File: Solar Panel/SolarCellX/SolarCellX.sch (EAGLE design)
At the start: 55 parts

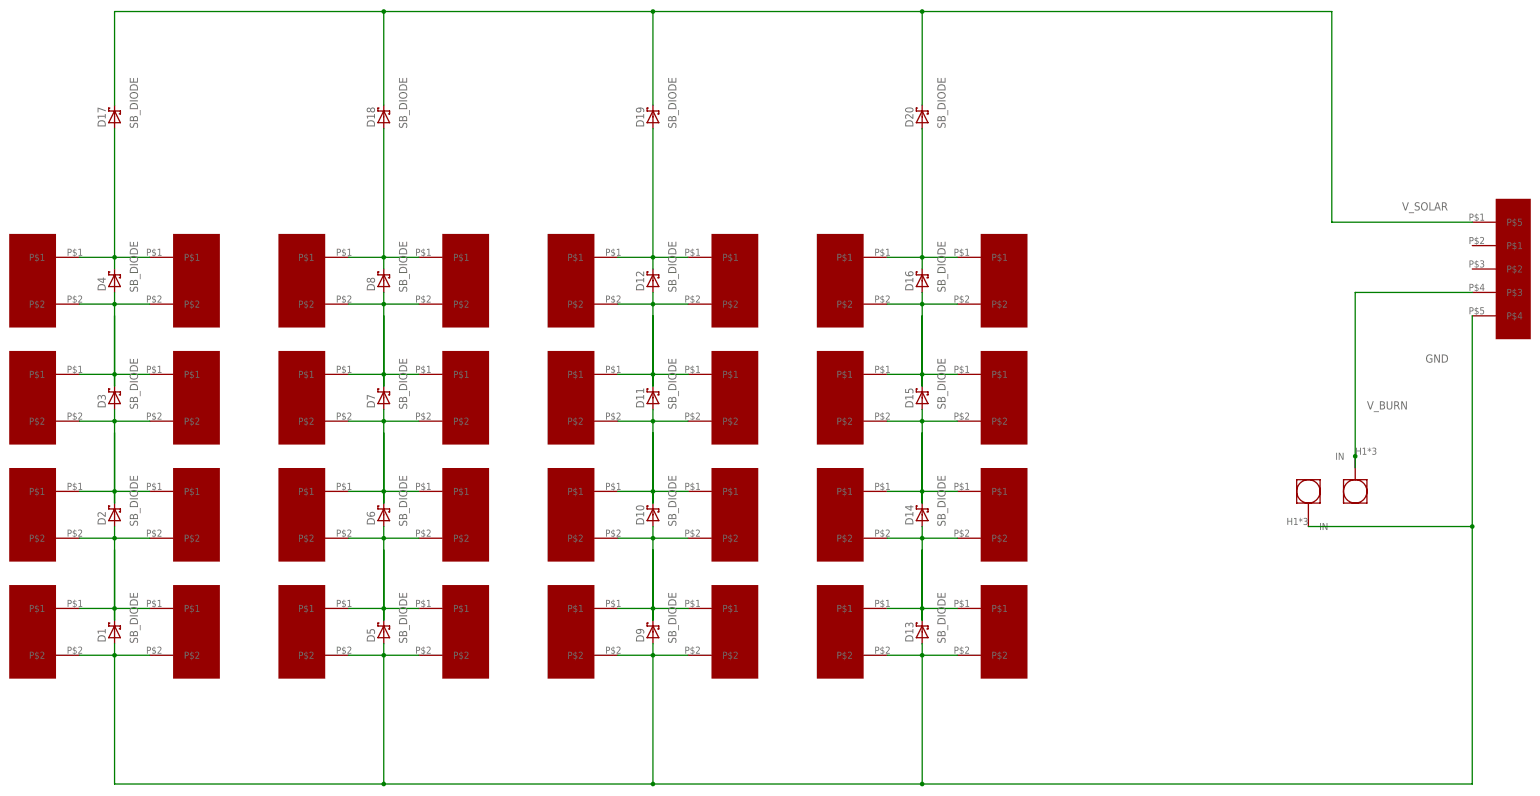
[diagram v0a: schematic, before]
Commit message: Updated Solar Panel with Alex's new sizes
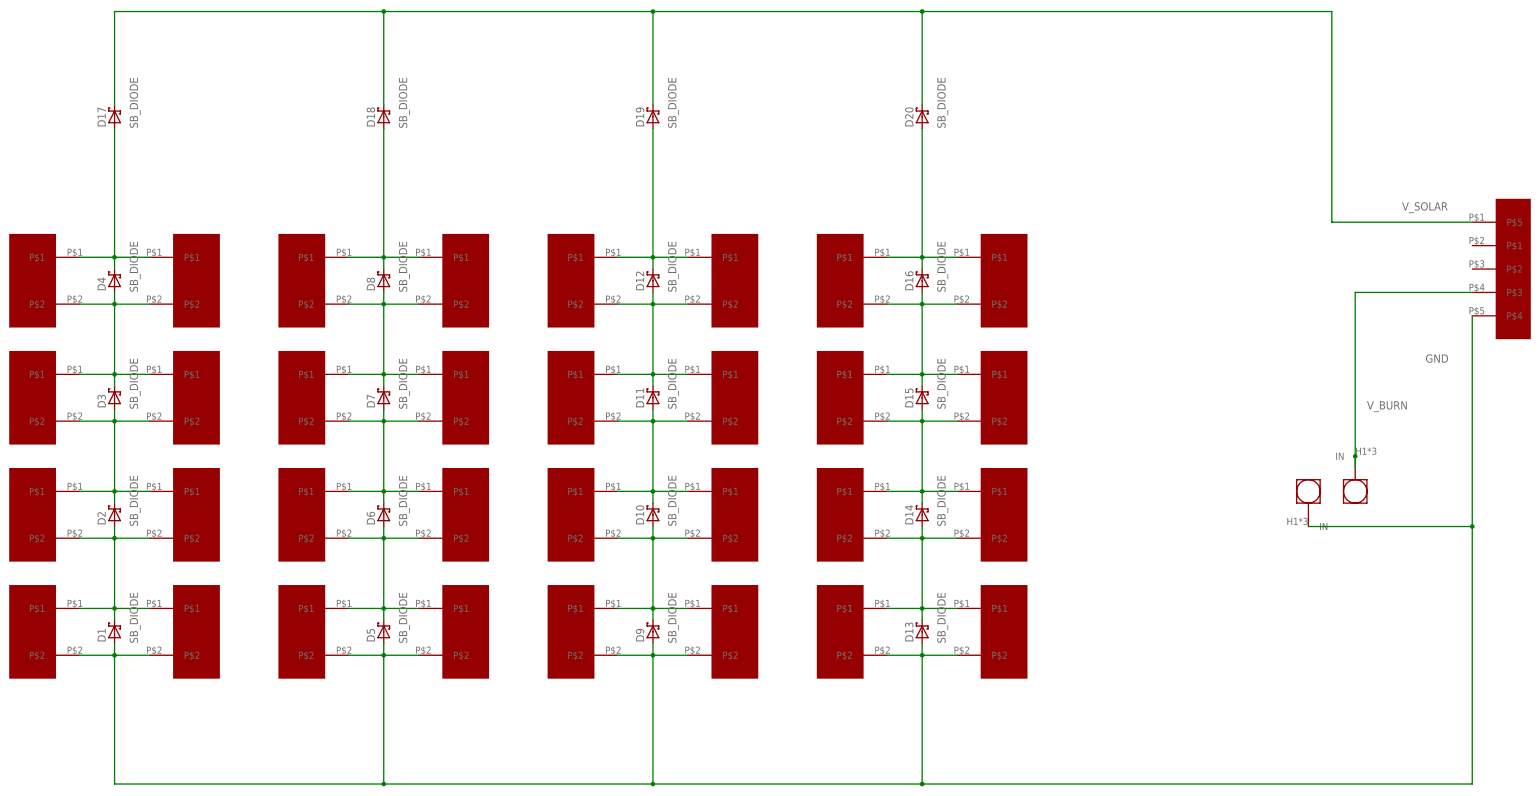
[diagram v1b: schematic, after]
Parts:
- renumbered SLR11 to 11, SLR12 to 12, SLR13 to 13, SLR14 to 14, SLR15 to 15, SLR16 to 16, SLR17 to 17, SLR18 to 18, U$10 to 21, U$11 to 24, U$12 to 23, U$13 to 26, U$14 to 25, U$15 to 28, U$16 to 27, U$17 to 32, U$18 to 31, U$19 to 34, U$20 to 33, U$21 to 36, U$22 to 35, U$23 to 38, U$24 to 37, U$25 to 42, U$26 to 41, U$27 to 44, U$28 to 43, U$29 to 46, U$30 to 45, U$31 to 48, U$32 to 47, U$9 to 22
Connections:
- removed net N$11: 23.P$2, 24.P$2, D6.POS
- removed net N$12: 23.P$1, 24.P$1, D6.NEG
- removed net N$13: 25.P$2, 26.P$2, D7.POS
- removed net N$15: 27.P$2, 28.P$2, D8.POS
- removed net N$19: 33.P$2, 34.P$2, D10.POS
- removed net N$21: 35.P$2, 36.P$2, D11.POS
- removed net N$23: 37.P$2, 38.P$2, D12.POS
- removed net N$27: 43.P$2, 44.P$2, D14.POS
- removed net N$29: 45.P$2, 46.P$2, D15.POS
- removed net N$3: 13.P$2, 14.P$2, D2.POS
- removed net N$31: 47.P$2, 48.P$2, D16.POS
- removed net N$5: 15.P$2, 16.P$2, D3.POS
- removed net N$7: 17.P$2, 18.P$2, D4.POS
- new net N$9: 23.P$1, 24.P$1, 25.P$2, 26.P$2, D6.NEG, D7.POS
- net N$10: now also 23.P$2, 24.P$2, D6.POS
- net N$14: now also 27.P$2, 28.P$2, D8.POS
- net N$18: now also 33.P$2, 34.P$2, D10.POS
- net N$2: now also 13.P$2, 14.P$2, D2.POS
- net N$20: now also 35.P$2, 36.P$2, D11.POS
- net N$22: now also 37.P$2, 38.P$2, D12.POS
- net N$26: now also 43.P$2, 44.P$2, D14.POS
- net N$28: now also 45.P$2, 46.P$2, D15.POS
- net N$30: now also 47.P$2, 48.P$2, D16.POS
- net N$4: now also 15.P$2, 16.P$2, D3.POS
- net N$6: now also 17.P$2, 18.P$2, D4.POS
